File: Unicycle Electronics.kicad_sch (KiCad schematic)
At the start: 20 parts, among them J1 USB_C, Q1 AO3402, SW1 PTS526SMG15SMTR2, SW2 PTS526SMG15SMTR2, U2 ESP32-C6-MINI-1/U, U3 AMS1117-3.3

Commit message: Finished Schematic, Started PCB
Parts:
- removed D1, D2: BXRE-30G20F0-C-83, symbol Device:LED
- removed Led: Rear LED 12V, symbol Device:LED
- removed R4: 5.1k, symbol Device:R
- added J2, J7: Tail Light, Connector_AMASS:AMASS_XT30PW-F_1x02_P2.50mm_Horizontal, symbol Connector_Generic:Conn_01x02
- added J3: BT1, Connector_JST:JST_PH_S2B-PH-K_1x02_P2.00mm_Horizontal, symbol Connector_Generic:Conn_01x02
- added J4: BT2, Connector_JST:JST_PH_S2B-PH-K_1x02_P2.00mm_Horizontal, symbol Connector_Generic:Conn_01x02
- added J5: BT3, Connector_JST:JST_PH_S2B-PH-K_1x02_P2.00mm_Horizontal, symbol Connector_Generic:Conn_01x02
- added J6: UART, Connector_JST:JST_PH_S3B-PH-K_1x03_P2.00mm_Horizontal, symbol Connector_Generic:Conn_01x03
- added R5: 4.7k, Resistor_SMD:R_1206_3216Metric, symbol Device:R
- added R6: 380, Resistor_SMD:R_1206_3216Metric, symbol Device:R
- added R7, R9: 0, Resistor_SMD:R_1206_3216Metric, symbol Device:R
- added R8: 5.1k, Resistor_SMD:R_1206_3216Metric, symbol Device:R
- added U1: PC817, Package_DIP:DIP-4_W7.62mm, symbol Isolator:PC817
- C1, C2, C3, C4: footprint (none) -> Capacitor_SMD:C_1206_3216Metric
- J1: renamed from 2 pin connector; footprint (none) -> Connector_AMASS:AMASS_XT30PW-M_1x02_P2.50mm_Horizontal
- J10: renamed from J1; footprint (none) -> Connector_USB:USB_C_Receptacle_GCT_USB4110; symbol Connector:USB_C_Receptacle_USB2.0 -> Connector:USB_C_Receptacle_USB2.0_14P
- LED DRIVER1: renamed from LED DRIVER; value LDH-45A-700 -> LDH-45A-500; footprint (none) -> Unicycle:LDH-45A-500
- R1, R2, R3, R4: footprint (none) -> Resistor_SMD:R_1206_3216Metric
- SW1, SW2: footprint (none) -> Button_Switch_SMD:SW_SPST_SKQG_WithStem
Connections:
- net +12V: now also J1.2 (Pin_2), J2.2 (Pin_2); no longer J1.1 (Pin_1)
- net +3.3V: now also R1.2, R5.1; no longer R1.1
- net GND: now also C3.1, J1.1 (Pin_1), J3.2 (Pin_2), J4.2 (Pin_2), J5.2 (Pin_2), J6.3 (Pin_3), R8.1, U1.2; no longer C3.2, J1.2 (Pin_2), LED DRIVER1.4 (Dim+)
- net at J10.A5 (CC1): now also R4.1
- net at SW2.2, U2.8 (EN/CHIP_PU): now also C3.2, R1.1; no longer C3.1, R1.2
- net at Q1.3 (D): now also J2.1 (Pin_1)
- net at LED DRIVER1.5 (PWM): now also R7.1, R9.1
- net at J10.B5 (CC2): now also R8.2; no longer R4.1
- net at LED DRIVER1.6 (Vout-): now also J7.1 (Pin_2)
- net BT1: now reaches U2.24 (GPIO18)
- net BT1: now also J3.1 (Pin_1)
- net BT2: now reaches U2.25 (GPIO19)
- net BT2: now also J4.1 (Pin_1)
- net BT3: now reaches U2.26 (GPIO20)
- net BT3: now also J5.1 (Pin_1)
- net RXD0: now reaches U2.30 (U0RXD/GPIO17)
- net RXD0: now also J6.1 (Pin_1)
- net TXD0: now reaches U2.31 (U0TXD/GPIO16)
- net TXD0: now also J6.2 (Pin_2)
- net GPIO2/ADC1_CH2 renamed Tail_Dimming
- net GPIO9 renamed BOOT
- net MTMS/GPIO4/ADC1_CH4 renamed DIM-
- net DIM-: now also U1.3; no longer U2.9 (MTMS/GPIO4/ADC1_CH4)
- new net: R6.1, U1.1
- new net: R5.2, R9.2, U1.4
- new net: J7.2 (Pin_1), LED DRIVER1.7 (Vout+)
- new net Head_Dimming: R6.2, R7.2, U2.9 (MTMS/GPIO4/ADC1_CH4)
- no-connect marks 0 -> 12
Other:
- note added: "I/O"
- note removed: "5.1k CC resistors for USB-C to USB-C cable support"
- note removed: "Changes I made: Updated EN pin schematic based on https://documentation.espressif.com/esp32-c6-mini-1_mini-1u_datasheet_en.pdf page 40 Added 3.3v connection for ESP32 and 22uF capacitor. I think it also needs a 10uF, i'll have to check"
- note removed: "EN/Reset Button"
- note removed: "TODO: USBC Port to the two USB pins. Also, you need to add two resistors to the USB-C port to specify that it's 5V so it works with C to C cables Flush out PWM Dimming Control (This is tail lights only, headlight dimming is done with pwm dimming pin & ESP32 Add all pins to LDH-65-700 Symbol (even unused ones) 12V Stepdown is not placed, needs to be removed from the schematic. It's an external dev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"
- moved on the sheet: C1, C2, C3, LED DRIVER1, Q1, R1, R2, R3, R4, SW1, SW2

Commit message: PCB Revision 1
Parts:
- J7: value Tail Light -> Headlight
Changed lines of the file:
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@@
 			)
 		)
-		(property "Value" "Tail Light"
+		(property "Value" "Headlight"
 			(at 193.04 115.5699 90)
 			(effects

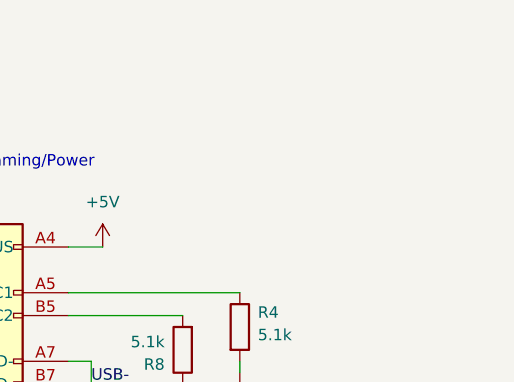
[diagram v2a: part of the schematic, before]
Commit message: Added mounting holes, updated footprints
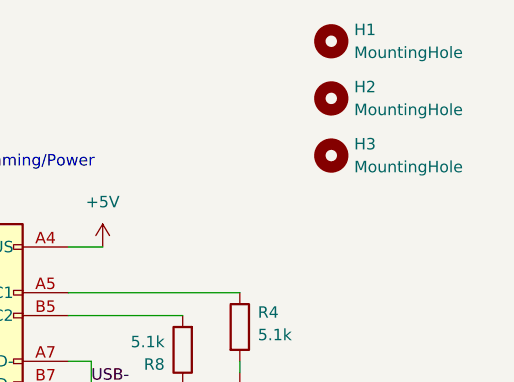
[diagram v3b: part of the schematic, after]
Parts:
- added H1, H2, H3: MountingHole, MountingHole:MountingHole_3.2mm_M3_DIN965_Pad, symbol Mechanical:MountingHole
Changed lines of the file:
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@@
+	)
+	(symbol
+		(lib_id "Mechanical:MountingHole")
+		(at 264.16 19.05 0)
+		(unit 1)
+		(exclude_from_sim no)
+		(in_bom no)
+		(on_board yes)
+		(dnp no)
+		(fields_autoplaced yes)
+		(property "Reference" "H1"
+			(at 266.7 17.7799 0)
+			(effects
+				(font
+					(size 1.27 1.27)
+				)
+				(justify left)
+			)
+		)
+		(property "Value" "MountingHole"
+			(at 266.7 20.3199 0)
+			(effects
+				(font
+					(size 1.27 1.27)
+				)
+				(justify left)
+			)
+		)
+		(property "Footprint" "MountingHole:MountingHole_3.2mm_M3_DIN965_Pad"
+			(at 264.16 19.05 0)
+			(effects
+				(font
+					(size 1.27 1.27)
+				)
+				(hide yes)
+			)
+		)
+		(property "Datasheet" "~"
+			(at 264.16 19.05 0)
+			(effects
+				(font
+					(size 1.27 1.27)
+				)
+				(hide yes)
+			)
+		)
+		(property "Description" "Mounting Hole without connection"
+			(at 264.16 19.05 0)
+			(effects
+				(font
+					(size 1.27 1.27)
+				)
+				(hide yes)
+			)
+		)
+		(instances
+			(project ""
+				(path "/ec3276b7-5d55-49ff-87c5-86105b5f1dbf"
+					(reference "H1")
+					(unit 1)
+				)
+			)
+		)
 	)
 	(symbol
@@
 	)
 	(symbol
+		(lib_id "Mechanical:MountingHole")
+		(at 264.16 31.75 0)
+		(unit 1)
+		(exclude_from_sim no)
+		(in_bom no)
+		(on_board yes)
+		(dnp no)
+		(fields_autoplaced yes)
+		(property "Reference" "H3"
+			(at 266.7 30.4799 0)
+			(effects
+				(font
+					(size 1.27 1.27)
+				)
+				(justify left)
+			)
+		)
+		(property "Value" "MountingHole"
+			(at 266.7 33.0199 0)
+			(effects
+				(font
+					(size 1.27 1.27)
+				)
+				(justify left)
+			)
+		)
+		(property "Footprint" "MountingHole:MountingHole_3.2mm_M3_DIN965_Pad"
+			(at 264.16 31.75 0)
+			(effects
+				(font
+					(size 1.27 1.27)
+				)
+				(hide yes)
+			)
+		)
+		(property "Datasheet" "~"
+			(at 264.16 31.75 0)
+			(effects
+				(font
+					(size 1.27 1.27)
+				)
+				(hide yes)
+			)
+		)
+		(property "Description" "Mounting Hole without connection"
+			(at 264.16 31.75 0)
+			(effects
+				(font
+					(size 1.27 1.27)
+				)
+				(hide yes)
+			)
+		)
+		(instances
+			(project "Unicycle Electronics"
+				(path "/ec3276b7-5d55-49ff-87c5-86105b5f1dbf"
+					(reference "H3")
+					(unit 1)
+				)
+			)
+		)
+	)
+	(symbol
 		(lib_id "power:+12V")
 		(at 97.79 143.51 0)
@@
 					(unit 1)
 				)
+			)
+		)
+	)
+	(symbol
+		(lib_id "Mechanical:MountingHole")
+		(at 264.16 25.4 0)
+		(unit 1)
+		(exclude_from_sim no)
+		(in_bom no)
+		(on_board yes)
+		(dnp no)
+		(fields_autoplaced yes)
+		(property "Reference" "H2"
+			(at 266.7 24.1299 0)
+			(effects
+				(font
+					(size 1.27 1.27)
+				)
+				(justify left)
+			)
+		)
+		(property "Value" "MountingHole"
+			(at 266.7 26.6699 0)
+			(effects
+				(font
+					(size 1.27 1.27)
+				)
+				(justify left)
+			)
+		)
+		(property "Footprint" "MountingHole:MountingHole_3.2mm_M3_DIN965_Pad"
+			(at 264.16 25.4 0)
+			(effects
+				(font
+					(size 1.27 1.27)
+				)
+				(hide yes)
+			)
+		)
+		(property "Datasheet" "~"
+			(at 264.16 25.4 0)
+			(effects
+				(font
+					(size 1.27 1.27)
+				)
+				(hide yes)
+			)
+		)
+		(property "Description" "Mounting Hole without connection"
+			(at 264.16 25.4 0)
+			(effects
+				(font
+					(size 1.27 1.27)
+				)
+				(hide yes)
+			)
+		)
+		(instances
+			(project "Unicycle Electronics"
+				(path "/ec3276b7-5d55-49ff-87c5-86105b5f1dbf"
+					(reference "H2")
+					(unit 1)
+				)

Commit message: Fixed footprint and routing for tail light MOSFET
gate and source were switched, incorrect footprint :(
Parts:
- Q1: footprint Package_TO_SOT_SMD:SOT-23 -> Unicycle:AO3402
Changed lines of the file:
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@@
 			)
 		)
-		(property "Footprint" "Package_TO_SOT_SMD:SOT-23"
+		(property "Footprint" "Unicycle:AO3402"
 			(at 100.33 155.575 0)
 			(effects

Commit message: updated 3d models
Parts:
- J1: footprint Connector_AMASS:AMASS_XT30PW-M_1x02_P2.50mm_Horizontal -> Unicycle:AMASS_XT30PW-M_1x02_P2.50mm_Horizontal
- J2, J7: footprint Connector_AMASS:AMASS_XT30PW-F_1x02_P2.50mm_Horizontal -> Unicycle:AMASS_XT30PW-F_1x02_P2.50mm_Horizontal
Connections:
- net GND: now also J10.SH (SHIELD); no longer J10.S1 (SHIELD)
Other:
- moved on the sheet: J7, LED DRIVER1, R5, R6, R7, R9, U1
